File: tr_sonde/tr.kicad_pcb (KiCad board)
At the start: 4 copper layers, 108.2 x 67.3 mm, 87 parts, among them J1 SMA, J2 SMA, J3 SMA, K1 SMDHDR, K2 SMDHDR, K3 SMDHDR, Q3 STD2NK90ZT4, Q4 STD2NK90ZT4, U1 L6388E, U2 75451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

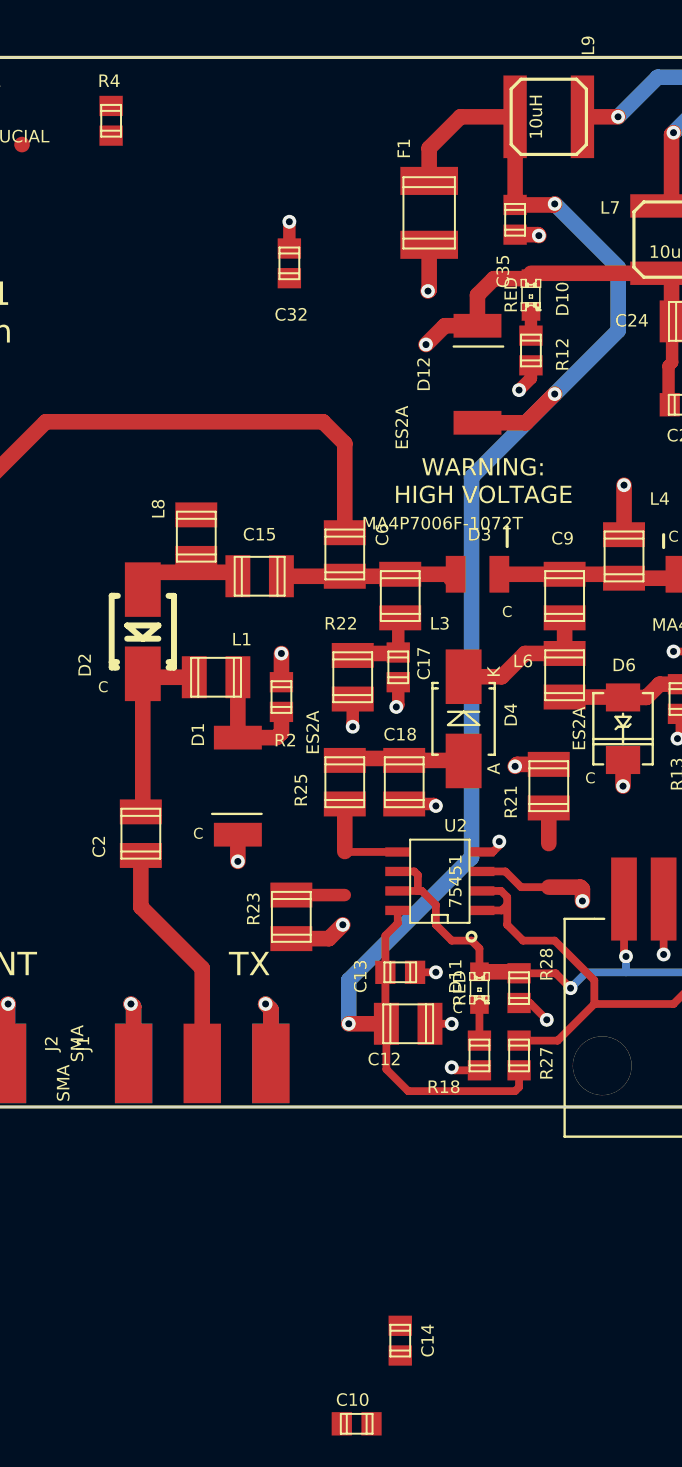
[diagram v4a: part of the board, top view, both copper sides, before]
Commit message: added digikey bom for driver amplifier production run
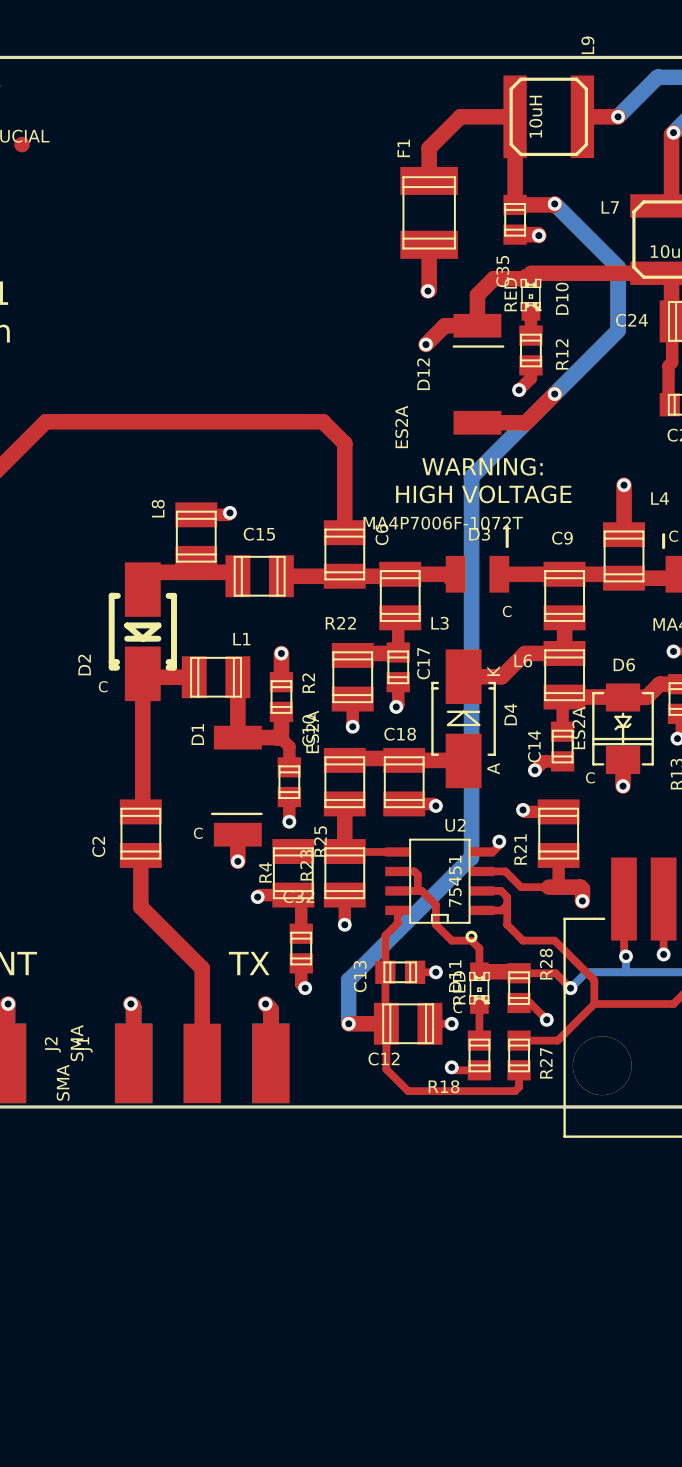
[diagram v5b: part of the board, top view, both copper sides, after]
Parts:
- R4: footprint smd_capacitors:c_0805 -> smd_capacitors:c_1210
- moved R4 49.7 mm to (87.4, 76.5)
- moved C32 43.9 mm to (87.9, 81.3), turned to 270 degrees
- moved C10 41.4 mm to (87.1, 70.6), turned to 270 degrees
- moved C14 39.5 mm to (104.6, 68.3), turned to 90 degrees
- moved R23 4.42 mm to (90.7, 76.5)
- moved R21 3.11 mm to (104.4, 73.9)
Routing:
- net Net-(C32-Pad2): track 0.08 -> 33.9 mm, vias 0 -> 2
- net GND: track 128.5 -> 132.1 mm, vias 46 -> 48
- net /TXDRV: track 9.76 -> 6.33 mm
- net Net-(C10-Pad2): track 8.31 -> 11.1 mm
- net Net-(C14-Pad1): track 7.73 -> 10.0 mm
- net VCC: track 154.3 -> 153.0 mm

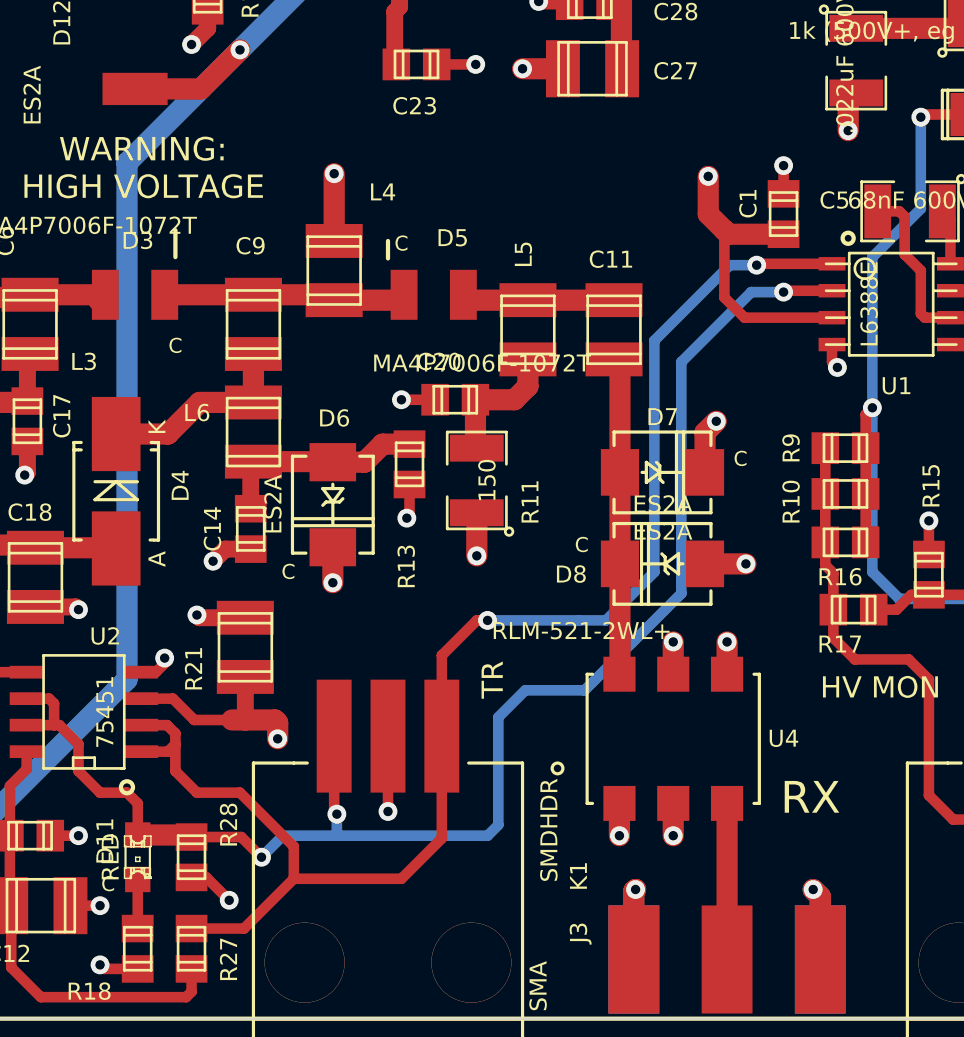
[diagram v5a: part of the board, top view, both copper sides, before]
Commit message: updated schematic with distributor part numbers
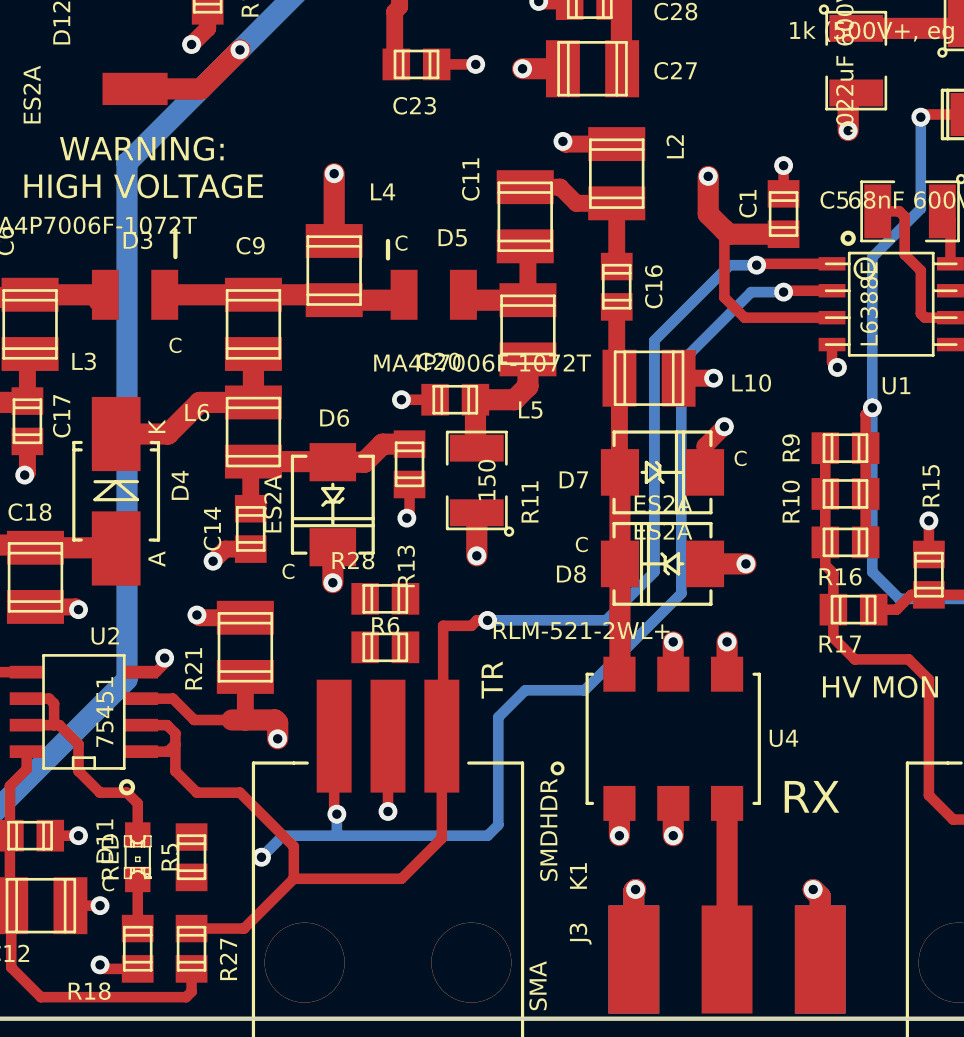
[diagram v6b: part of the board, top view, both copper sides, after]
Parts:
- added C16: 330 pF, smd_capacitors:c_0805, F.Cu at (121.9, 56.9)
- added L10: 22uH, smd_capacitors:c_1210, F.Cu at (123.4, 61.2)
- added L2: 22uH, smd_capacitors:c_1210, F.Cu at (121.9, 51.6)
- added R5: 10k, smd_capacitors:c_0805, F.Cu at (101.9, 83.8)
- added R6: 10k, smd_capacitors:c_0805, F.Cu at (111.0, 73.9)
- R21, R23, R4: value 150 -> 100
- moved R28 15.2 mm to (111.0, 71.6), turned to 0 degrees
- moved C11 6.78 mm to (117.6, 53.6), turned to 270 degrees
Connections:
- D7 pad 1: Net-(C11-Pad2) -> Net-(C16-Pad1)
- D8 pad 2: Net-(C11-Pad2) -> Net-(C16-Pad1)
- U4 pad 1: Net-(C11-Pad2) -> Net-(C16-Pad1)
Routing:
- net Net-(C16-Pad1): track 0.00 -> 17.4 mm
- net Net-(C11-Pad2): track 15.0 -> 7.62 mm
- net /TX: track 70.0 -> 63.7 mm
- net GND: track 132.1 -> 134.0 mm, vias 48 -> 49
- net Net-(C11-Pad1): track 7.21 -> 5.74 mm
- net /RX: track 68.8 -> 69.5 mm

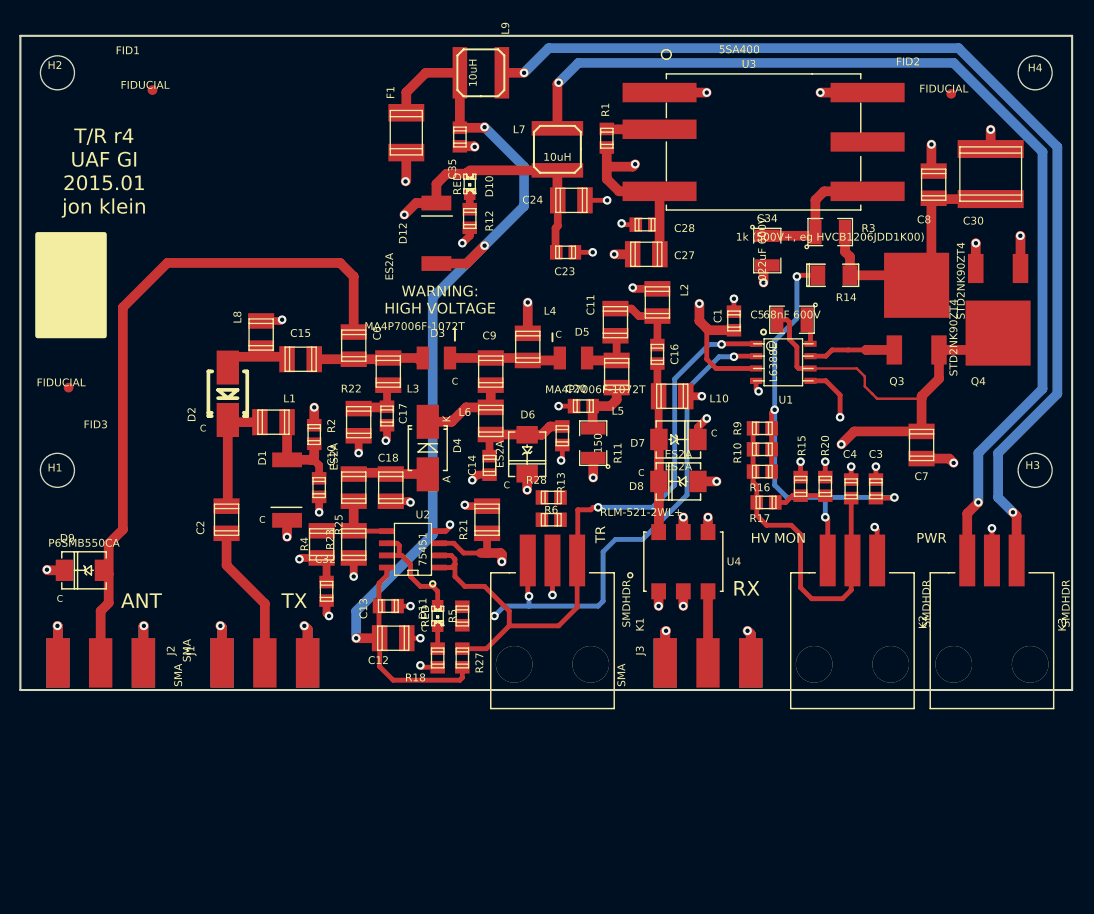
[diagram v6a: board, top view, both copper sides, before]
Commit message: modified hptr for higher power resistors
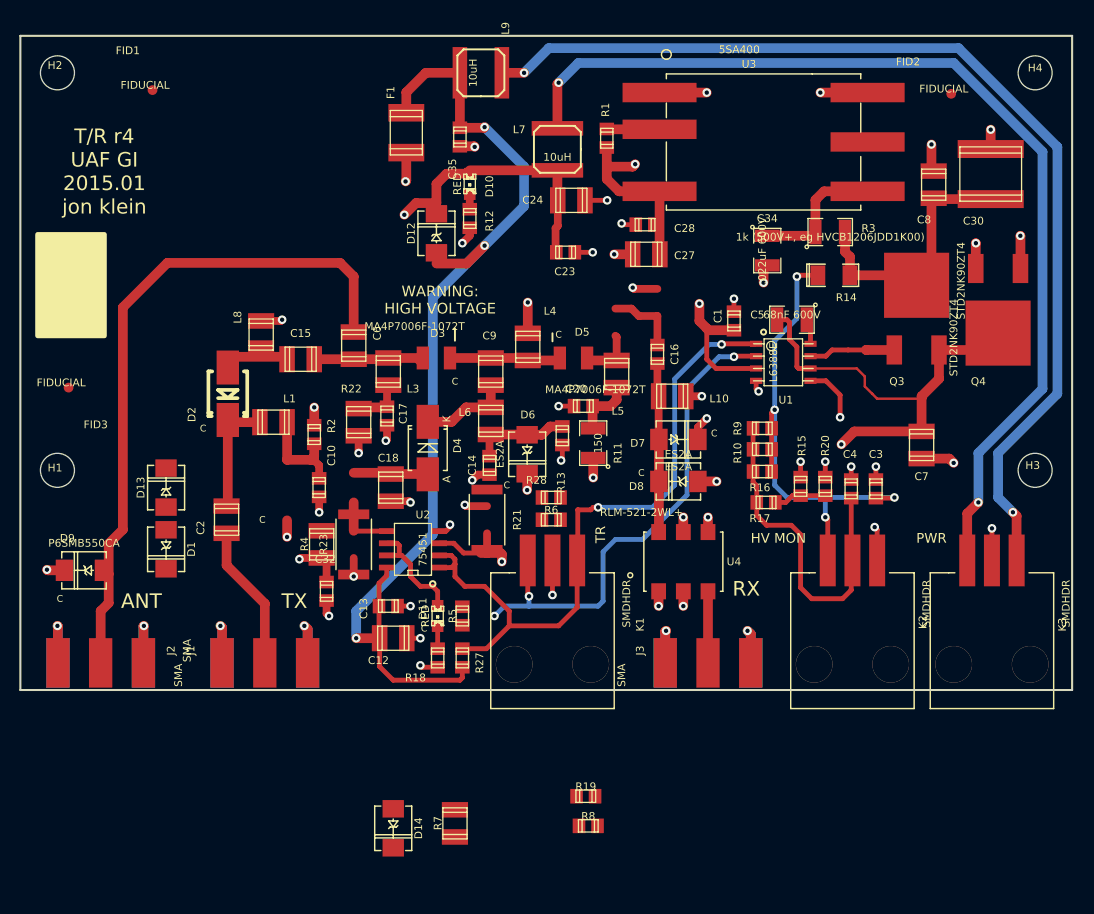
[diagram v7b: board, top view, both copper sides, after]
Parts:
- removed C11: .022uF 600V, smd_capacitors:c_1210
- removed L2: 22uH, smd_capacitors:c_1210
- removed R25: 150, smd_capacitors:c_1210
- added D13: ES2A, SMD_Packages:DO-214-AA_SMB, F.Cu at (71.4, 70.6)
- added D14: ES2A, SMD_Packages:DO-214-AA_SMB, F.Cu at (94.7, 105.7)
- added R19: 1k, smd_capacitors:c_0805, F.Cu at (114.6, 102.4)
- added R7: 150, smd_capacitors:c_1210, F.Cu at (101.1, 105.2)
- added R8: 1k, smd_capacitors:c_0805, F.Cu at (114.8, 105.4)
- C16: value 330 pF -> 470 pF
- D1, D12: footprint smb_diode:SMB_DO2144AA -> SMD_Packages:DO-214-AA_SMB
- R21, R23: value 100 -> 150; footprint smd_capacitors:c_1210 -> Resistors_SMD:R_2512
- R4: value 100 -> 150
- moved D1 13.9 mm to (71.4, 77.0)
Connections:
- C16 pad 2: Net-(C11-Pad2) -> Net-(C16-Pad2)
- D1 pad 2: GND -> Net-(D1-Pad2)
- D5 pad 1: Net-(C11-Pad1) -> Net-(C16-Pad2)
- D6 pad 2: GND -> Net-(D14-Pad1)
- L5 pad 2: Net-(C11-Pad1) -> Net-(C16-Pad2)
- R23 pad 1: /TXDRV -> VCC
- R23 pad 2: VCC -> /TXDRV
- U3 pad 5: (no net) -> Net-(U3-Pad5)
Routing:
- net VCC: track 153.0 -> 208.3 mm, vias 6 -> 9
- net /RXDRV: track 60.2 -> 4.93 mm, vias 3 -> 0
- net Net-(C16-Pad2): track 0.00 -> 13.4 mm
- net Net-(C11-Pad2): track 7.62 -> 0.00 mm
- net GND: track 134.0 -> 128.0 mm, vias 49 -> 46
- net Net-(C11-Pad1): track 5.74 -> 0.00 mm
- net (no net): track 0.00 -> 4.31 mm, vias 0 -> 2
- net Net-(D14-Pad1): track 0.00 -> 1.68 mm, vias 0 -> 1

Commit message: committing modified files, I forget.., probably dfm
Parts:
- moved R7 57.8 mm to (82.3, 50.5), turned to 0 degrees
- moved R8 44.8 mm to (91.2, 67.3)
- moved R19 40.2 mm to (91.2, 69.6)
- moved D14 37.3 mm to (108.7, 71.1)
- moved C32 33.2 mm to (78.2, 49.5), turned to 90 degrees
- moved R4 29.9 mm to (82.3, 47.0), turned to 0 degrees
- moved D13 14.5 mm to (83.8, 78.0), turned to 270 degrees
- moved D1 14.0 mm to (83.8, 70.6)
- moved R28 8.52 mm to (118.6, 75.4), turned to 90 degrees
- moved R6 5.55 mm to (116.3, 75.4), turned to 90 degrees
- moved R5 4.26 mm to (103.1, 87.9)
- moved D6 2.67 mm to (108.7, 64.5)
- moved R23 1.61 mm to (90.2, 74.9)
- moved R27 1.05 mm to (100.8, 87.9)
- moved D11 1.02 mm to (98.3, 83.8)
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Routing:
- net /RXDRV: track 4.93 -> 62.3 mm, vias 0 -> 3
- net VCC: track 208.3 -> 154.4 mm, vias 9 -> 6
- net /TXDRV: track 6.33 -> 36.5 mm, vias 0 -> 2
- net Net-(C32-Pad2): track 33.9 -> 9.28 mm, vias 2 -> 0
- net /TX: track 63.7 -> 76.3 mm, vias 3 -> 4
- net GND: track 128.0 -> 137.4 mm, vias 46 -> 50
- net Net-(C6-Pad2): track 69.8 -> 77.6 mm
- net Net-(C16-Pad2): track 13.4 -> 7.94 mm
- net +5V: track 107.0 -> 110.7 mm
- net Net-(D1-Pad2): track 0.00 -> 3.35 mm
- net Net-(C14-Pad1): track 10.0 -> 12.8 mm
- net (no net): track 4.31 -> 2.59 mm, vias 2 -> 1
- net Net-(C18-Pad1): track 7.69 -> 8.80 mm
- net Net-(D14-Pad1): track 1.68 -> 2.59 mm, vias 1 -> 0
- net /RX: track 69.5 -> 69.0 mm
